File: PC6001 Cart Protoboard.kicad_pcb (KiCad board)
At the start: 2 copper layers, 97.8 x 80.6 mm, 13 parts, among them J1 PC-6001 edge connector, SW1 PicoReset, SW2 EspReset, U2 ESP32-DevKitC, U3 74LS32

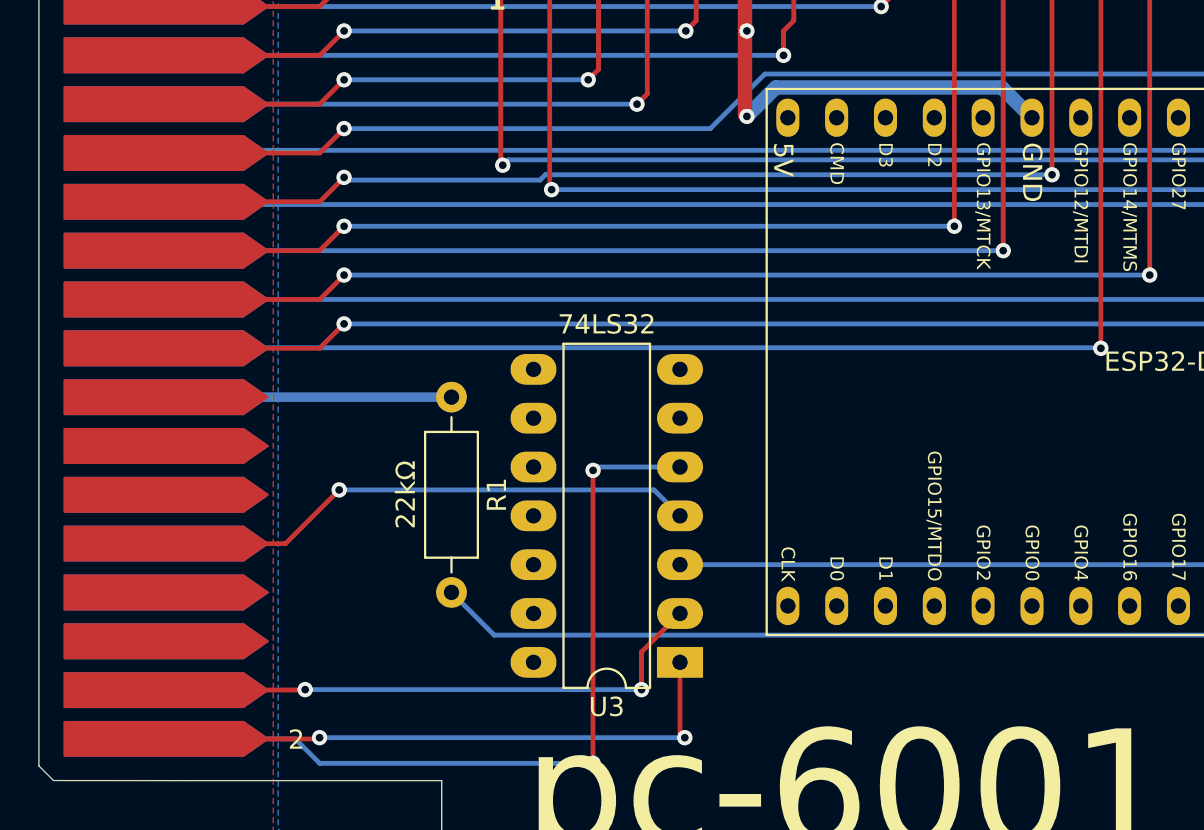
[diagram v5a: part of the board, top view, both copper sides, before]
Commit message: TEMPORARILY putting SRAM in the ESP
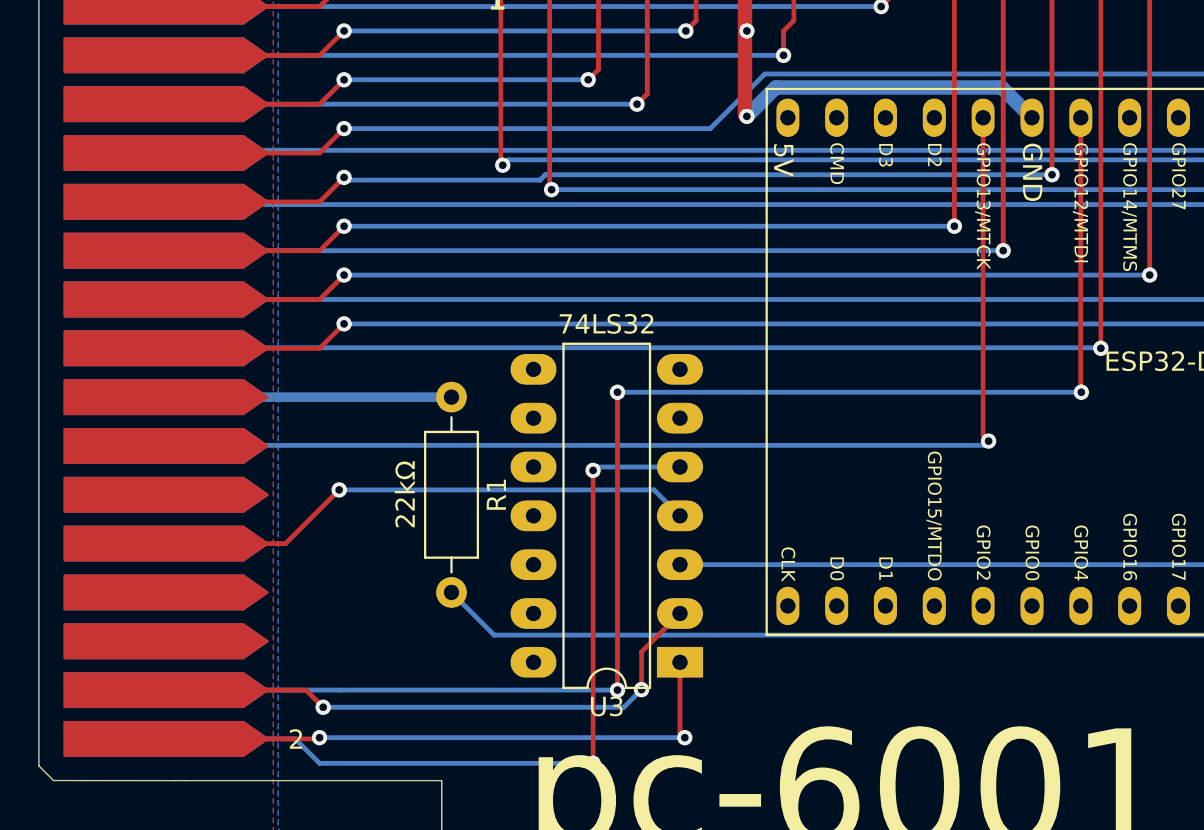
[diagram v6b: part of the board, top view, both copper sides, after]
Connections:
- U2 pad 13: unconnected-(U2-MTDI/GPIO12/ADC2_CH5-Pad13) -> /~{DRD2}
- U2 pad 15: unconnected-(U2-MTCK/GPIO13/ADC2_CH4-Pad15) -> /~{WR}
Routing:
- net /~{DRD2}: track 0.00 -> 80.8 mm, vias 0 -> 3
- net /~{WR}: track 0.00 -> 63.3 mm, vias 0 -> 1
- net /~{CS2}: track 33.0 -> 33.7 mm
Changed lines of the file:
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@@
 	(net 74 "unconnected-(U2-U0RXD{slash}GPIO3-Pad34)")
 	(net 75 "unconnected-(U2-SD_DATA3{slash}GPIO10-Pad17)")
-	(net 76 "unconnected-(U2-MTCK{slash}GPIO13{slash}ADC2_CH4-Pad15)")
-	(net 77 "unconnected-(U2-GPIO18-Pad30)")
-	(net 78 "unconnected-(U2-GPIO19-Pad31)")
-	(net 79 "/WIFI_LED")
-	(net 80 "unconnected-(U2-SD_DATA0{slash}GPIO7-Pad21)")
-	(net 81 "unconnected-(U2-MTMS{slash}GPIO14{slash}ADC2_CH6-Pad12)")
-	(net 82 "/CMD")
-	(net 83 "unconnected-(U2-VDET_2{slash}GPIO35{slash}ADC1_CH7-Pad6)")
-	(net 84 "unconnected-(U2-GPIO0{slash}BOOT{slash}ADC2_CH1-Pad25)")
-	(net 85 "unconnected-(U2-SENSOR_VN{slash}GPIO39{slash}ADC1_CH3-Pad4)")
-	(net 86 "unconnected-(U2-MTDI{slash}GPIO12{slash}ADC2_CH5-Pad13)")
-	(net 87 "unconnected-(U2-SD_DATA2{slash}GPIO9-Pad16)")
-	(net 88 "/ESP_RST")
-	(net 89 "unconnected-(U2-MTDO{slash}GPIO15{slash}ADC2_CH3-Pad23)")
-	(net 90 "+3.3V")
-	(net 91 "Net-(D1-K)")
-	(net 92 "/~{RAMSEL}")
+	(net 76 "unconnected-(U2-GPIO18-Pad30)")
+	(net 77 "unconnected-(U2-GPIO19-Pad31)")
+	(net 78 "/WIFI_LED")
+	(net 79 "unconnected-(U2-SD_DATA0{slash}GPIO7-Pad21)")
+	(net 80 "unconnected-(U2-MTMS{slash}GPIO14{slash}ADC2_CH6-Pad12)")
+	(net 81 "/CMD")
+	(net 82 "unconnected-(U2-VDET_2{slash}GPIO35{slash}ADC1_CH7-Pad6)")
+	(net 83 "unconnected-(U2-GPIO0{slash}BOOT{slash}ADC2_CH1-Pad25)")
+	(net 84 "unconnected-(U2-SENSOR_VN{slash}GPIO39{slash}ADC1_CH3-Pad4)")
+	(net 85 "unconnected-(U2-SD_DATA2{slash}GPIO9-Pad16)")
+	(net 86 "/ESP_RST")
+	(net 87 "unconnected-(U2-MTDO{slash}GPIO15{slash}ADC2_CH3-Pad23)")
+	(net 88 "+3.3V")
+	(net 89 "Net-(D1-K)")
+	(net 90 "/~{RAMSEL}")
 	(footprint "PC6001 Edge Connector:PC6001 Cartridge Connector"
 		(layer "F.Cu")
@@
 		(tags "Diode DO-35_SOD27 series Axial Horizontal pin pitch 7.62mm  length 4mm diameter 2mm")
 		(property "Reference" "D1"
-			(at 3.81 0 360)
+			(at 3.81 0 0)
 			(layer "F.SilkS")
 			(effects
@@
 		)
 		(property "Value" "D"
-			(at 3.81 2.12 360)
+			(at 3.81 2.12 0)
 			(layer "F.Fab")
 			(effects
@@
 		)
 		(fp_text user "${REFERENCE}"
-			(at 4.11 0 360)
+			(at 4.11 0 0)
 			(layer "F.Fab")
 			(effects
@@
 			(layers "*.Cu" "*.Mask")
 			(remove_unused_layers no)
-			(net 91 "Net-(D1-K)")
+			(net 89 "Net-(D1-K)")
 			(pinfunction "K")
 			(pintype "passive")
@@
 			(layers "*.Cu" "*.Mask")
 			(remove_unused_layers no)
-			(net 88 "/ESP_RST")
+			(net 86 "/ESP_RST")
 			(pinfunction "A")
 			(pintype "passive")
@@
 			(layers "*.Cu" "*.Mask")
 			(remove_unused_layers no)
-			(net 91 "Net-(D1-K)")
+			(net 89 "Net-(D1-K)")
 			(pinfunction "2")
 			(pintype "passive")
@@
 			(layers "*.Cu" "*.Mask")
 			(remove_unused_layers no)
-			(net 91 "Net-(D1-K)")
+			(net 89 "Net-(D1-K)")
 			(pinfunction "2")
 			(pintype "passive")
@@
 			(layers "*.Cu" "*.Mask")
 			(remove_unused_layers no)
-			(net 90 "+3.3V")
+			(net 88 "+3.3V")
 			(pinfunction "3V3")
 			(pintype "power_in")
@@
 			(layers "*.Cu" "*.Mask")
 			(remove_unused_layers no)
-			(net 88 "/ESP_RST")
+			(net 86 "/ESP_RST")
 			(pinfunction "CHIP_PU")
 			(pintype "input")
@@
 			(layers "*.Cu" "*.Mask")
 			(remove_unused_layers no)
-			(net 85 "unconnected-(U2-SENSOR_VN{slash}GPIO39{slash}ADC1_CH3-Pad4)")
+			(net 84 "unconnected-(U2-SENSOR_VN{slash}GPIO39{slash}ADC1_CH3-Pad4)")
 			(pinfunction "SENSOR_VN/GPIO39/ADC1_CH3")
 			(pintype "input")
@@
 			(layers "*.Cu" "*.Mask")
 			(remove_unused_layers no)
-			(net 83 "unconnected-(U2-VDET_2{slash}GPIO35{slash}ADC1_CH7-Pad6)")
+			(net 82 "unconnected-(U2-VDET_2{slash}GPIO35{slash}ADC1_CH7-Pad6)")
 			(pinfunction "VDET_2/GPIO35/ADC1_CH7")
 			(pintype "input")
@@
 			(layers "*.Cu" "*.Mask")
 			(remove_unused_layers no)
-			(net 82 "/CMD")
+			(net 81 "/CMD")
 			(pinfunction "DAC_1/ADC2_CH8/GPIO25")
 			(pintype "bidirectional")
@@
 			(layers "*.Cu" "*.Mask")
 			(remove_unused_layers no)
-			(net 81 "unconnected-(U2-MTMS{slash}GPIO14{slash}ADC2_CH6-Pad12)")
+			(net 80 "unconnected-(U2-MTMS{slash}GPIO14{slash}ADC2_CH6-Pad12)")
 			(pinfunction "MTMS/GPIO14/ADC2_CH6")
 			(pintype "bidirectional")
@@
 			(layers "*.Cu" "*.Mask")
 			(remove_unused_layers no)
-			(net 86 "unconnected-(U2-MTDI{slash}GPIO12{slash}ADC2_CH5-Pad13)")
+			(net 4 "/~{DRD2}")
 			(pinfunction "MTDI/GPIO12/ADC2_CH5")
 			(pintype "bidirectional")
@@
 			(layers "*.Cu" "*.Mask")
 			(remove_unused_layers no)
-			(net 76 "unconnected-(U2-MTCK{slash}GPIO13{slash}ADC2_CH4-Pad15)")
+			(net 45 "/~{WR}")
 			(pinfunction "MTCK/GPIO13/ADC2_CH4")
 			(pintype "bidirectional")
@@
 			(layers "*.Cu" "*.Mask")
 			(remove_unused_layers no)
-			(net 87 "unconnected-(U2-SD_DATA2{slash}GPIO9-Pad16)")
+			(net 85 "unconnected-(U2-SD_DATA2{slash}GPIO9-Pad16)")
 			(pinfunction "SD_DATA2/GPIO9")
 			(pintype "bidirectional")
@@
 			(layers "*.Cu" "*.Mask")
 			(remove_unused_layers no)
-			(net 80 "unconnected-(U2-SD_DATA0{slash}GPIO7-Pad21)")
+			(net 79 "unconnected-(U2-SD_DATA0{slash}GPIO7-Pad21)")
 			(pinfunction "SD_DATA0/GPIO7")
 			(pintype "bidirectional")
@@
 			(layers "*.Cu" "*.Mask")
 			(remove_unused_layers no)
-			(net 89 "unconnected-(U2-MTDO{slash}GPIO15{slash}ADC2_CH3-Pad23)")
+			(net 87 "unconnected-(U2-MTDO{slash}GPIO15{slash}ADC2_CH3-Pad23)")
 			(pinfunction "MTDO/GPIO15/ADC2_CH3")
 			(pintype "bidirectional")
@@
 			(layers "*.Cu" "*.Mask")
 			(remove_unused_layers no)
-			(net 79 "/WIFI_LED")
+			(net 78 "/WIFI_LED")
 			(pinfunction "ADC2_CH2/GPIO2")
 			(pintype "bidirectional")
@@
 			(layers "*.Cu" "*.Mask")
 			(remove_unused_layers no)
-			(net 84 "unconnected-(U2-GPIO0{slash}BOOT{slash}ADC2_CH1-Pad25)")
+			(net 83 "unconnected-(U2-GPIO0{slash}BOOT{slash}ADC2_CH1-Pad25)")
 			(pinfunction "GPIO0/BOOT/ADC2_CH1")
 			(pintype "bidirectional")
@@
 			(layers "*.Cu" "*.Mask")
 			(remove_unused_layers no)
-			(net 77 "unconnected-(U2-GPIO18-Pad30)")
+			(net 76 "unconnected-(U2-GPIO18-Pad30)")
 			(pinfunction "GPIO18")
 			(pintype "bidirectional")
@@
 			(layers "*.Cu" "*.Mask")
 			(remove_unused_layers no)
-			(net 78 "unconnected-(U2-GPIO19-Pad31)")
+			(net 77 "unconnected-(U2-GPIO19-Pad31)")
 			(pinfunction "GPIO19")
 			(pintype "bidirectional")
@@
 			(layers "*.Cu" "*.Mask")
 			(remove_unused_layers no)
-			(net 92 "/~{RAMSEL}")
+			(net 90 "/~{RAMSEL}")
 			(pintype "output")
 		)
@@
 			(layers "*.Cu" "*.Mask")
 			(remove_unused_layers no)
-			(net 88 "/ESP_RST")
+			(net 86 "/ESP_RST")
 			(pintype "passive")
 		)
@@
 	)
 	(segment
+		(start 174.85 121.002)
+		(end 174.85 106.75)
+		(width 0.25)
+		(layer "F.Cu")
+		(net 4)
+	)
+	(segment
+		(start 174.879 121.031)
+		(end 174.85 121.002)
+		(width 0.25)
+		(layer "F.Cu")
+		(net 4)
+	)
+	(segment
+		(start 150.749 136.525)
+		(end 150.749 121.031)
+		(width 0.25)
+		(layer "F.Cu")
+		(net 4)
+	)
+	(via
+		(at 150.749 136.525)
+		(size 0.8)
+		(drill 0.4)
+		(layers "F.Cu" "B.Cu")
+		(net 4)
+	)
+	(via
+		(at 174.879 121.031)
+		(size 0.8)
+		(drill 0.4)
+		(layers "F.Cu" "B.Cu")
+		(net 4)
+	)
+	(via
+		(at 150.749 121.031)
+		(size 0.8)
+		(drill 0.4)
+		(layers "F.Cu" "B.Cu")
+		(net 4)
+	)
+	(segment
+		(start 123.825 136.525)
+		(end 136.271 136.525)
+		(width 0.25)
+		(layer "B.Cu")
+		(net 4)
+	)
+	(segment
+		(start 136.271 136.525)
+		(end 150.749 136.525)
+		(width 0.25)
+		(layer "B.Cu")
+		(net 4)
+	)
+	(segment
+		(start 150.749 121.031)
+		(end 174.879 121.031)
+		(width 0.25)
+		(layer "B.Cu")
+		(net 4)
+	)
+	(segment
 		(start 142.113 121.285)
 		(end 123.825 121.285)
@@
 	)
 	(segment
-		(start 134.475 136.525)
-		(end 134.5 136.5)
+		(start 169.77 123.288)
+		(end 169.77 106.75)
 		(width 0.25)
 		(layer "F.Cu")
-		(net 47)
+		(net 45)
+	)
+	(segment
+		(start 170.053 123.571)
+		(end 169.77 123.288)
+		(width 0.25)
+		(layer "F.Cu")
+		(net 45)
+	)
+	(via
+		(at 170.053 123.571)
+		(size 0.8)
+		(drill 0.4)
+		(layers "F.Cu" "B.Cu")
+		(net 45)
+	)
+	(segment
+		(start 123.825 123.825)
+		(end 123.855 123.795)
+		(width 0.25)
+		(layer "B.Cu")
+		(net 45)
+	)
+	(segment
+		(start 123.855 123.795)
+		(end 169.829 123.795)
+		(width 0.25)
+		(layer "B.Cu")
+		(net 45)
+	)
+	(segment
+		(start 169.829 123.795)
+		(end 170.053 123.571)
+		(width 0.25)
+		(layer "B.Cu")
+		(net 45)
 	)
 	(segment
@@
 	(segment
 		(start 123.825 136.525)
-		(end 134.475 136.525)
+		(end 134.543789 136.525)
+		(width 0.25)
+		(layer "F.Cu")
+		(net 47)
+	)
+	(segment
+		(start 134.543789 136.525)
+		(end 135.437901 137.419112)
 		(width 0.25)
 		(layer "F.Cu")
@@
 	)
 	(via
-		(at 134.5 136.5)
+		(at 135.437901 137.419112)
 		(size 0.8)
 		(drill 0.4)
@@
 	)
 	(segment
-		(start 134.5 136.5)
-		(end 152 136.5)
+		(start 152 136.5)
+		(end 151.080888 137.419112)
+		(width 0.25)
+		(layer "B.Cu")
+		(net 47)
+	)
+	(segment
+		(start 151.080888 137.419112)
+		(end 135.437901 137.419112)
 		(width 0.25)
 		(layer "B.Cu")
@@
 		(width 0.25)
 		(layer "F.Cu")
-		(net 88)
+		(net 86)
 	)
 	(segment
@@
 		(width 0.25)
 		(layer "F.Cu")
-		(net 88)
+		(net 86)
 	)
 	(segment
@@
 		(width 0.25)
 		(layer "F.Cu")
-		(net 88)
+		(net 86)
 	)
 	(segment
@@
 		(width 0.25)
 		(layer "F.Cu")
-		(net 88)
+		(net 86)
 	)
 	(via
@@
 		(drill 0.4)
 		(layers "F.Cu" "B.Cu")
-		(net 88)
+		(net 86)
 	)
 	(segment
@@
 		(width 0.25)
 		(layer "B.Cu")
-		(net 88)
+		(net 86)
 	)
 	(segment
@@
 		(width 0.25)
 		(layer "B.Cu")
-		(net 88)
+		(net 86)
 	)
 	(segment
@@
 		(width 0.25)
 		(layer "B.Cu")
-		(net 88)
+		(net 86)
 	)
 	(segment
@@
 		(width 0.25)
 		(layer "F.Cu")
-		(net 91)
+		(net 89)
 	)
 	(segment
@@
 		(width 0.25)
 		(layer "F.Cu")
-		(net 91)
+		(net 89)
 	)
 	(segment
@@
 		(width 0.25)
 		(layer "B.Cu")
-		(net 91)
+		(net 89)
 	)
 	(zone

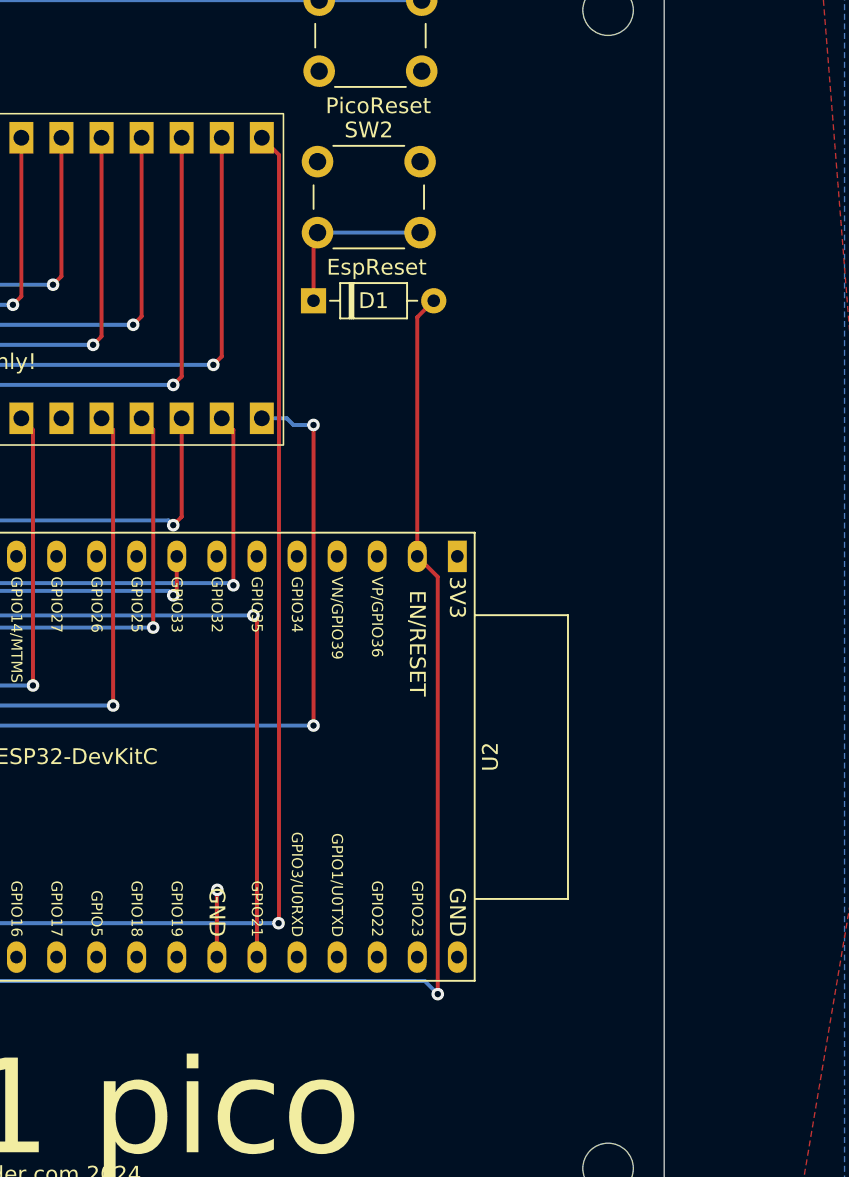
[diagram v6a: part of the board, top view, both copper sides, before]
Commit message: Added an AliExpress microSD card module
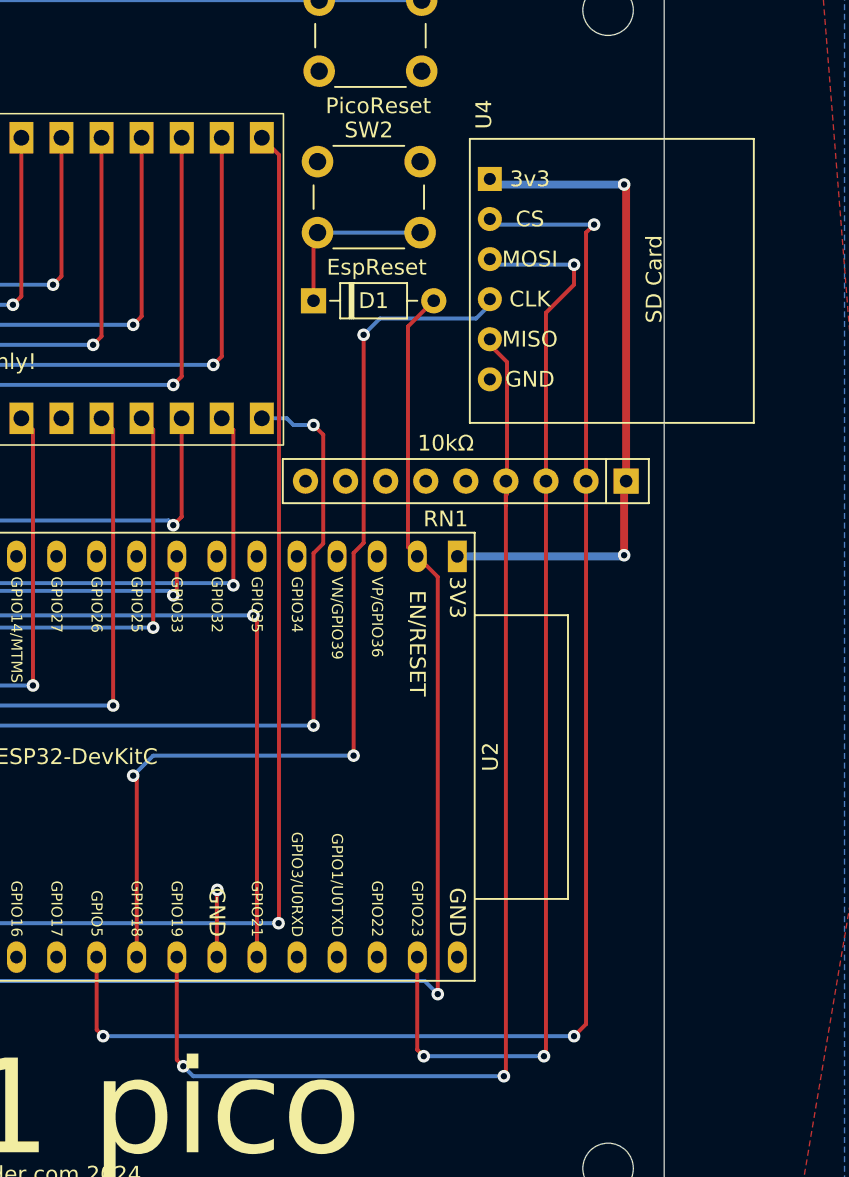
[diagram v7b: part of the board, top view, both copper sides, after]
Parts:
- added RN1: 10kΩ, Resistor_THT:R_Array_SIP9, F.Cu at (216.0, 102.0)
- added U4: microSD-Breakout, microSD_Breakout:microSD_AliExpress, F.Cu at (206.1, 80.3)
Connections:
- U2 pad 29: unconnected-(U2-GPIO5-Pad29) -> /IO5/~{SPI_CS}
- U2 pad 30: unconnected-(U2-GPIO18-Pad30) -> /IO18/SPI_CLK
- U2 pad 31: unconnected-(U2-GPIO19-Pad31) -> /IO19/SPI_MISO
- U2 pad 37: unconnected-(U2-GPIO23-Pad37) -> /IO23/SPI_MOSI
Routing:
- net /IO5/~{SPI_CS}: track 0.00 -> 93.6 mm, vias 0 -> 3
- net /IO19/SPI_MISO: track 0.00 -> 76.1 mm, vias 0 -> 2
- net /IO23/SPI_MOSI: track 0.00 -> 70.4 mm, vias 0 -> 3
- net /IO18/SPI_CLK: track 0.00 -> 61.8 mm, vias 0 -> 3
- net +3.3V: track 0.00 -> 42.7 mm, vias 0 -> 2
- net /a15: track 95.4 -> 95.9 mm

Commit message: Button A
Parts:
- added D2: Wifi, LED_THT:LED_D3.0mm, F.Cu at (214.6, 130.8)
- added D3: Bus, LED_THT:LED_D3.0mm, F.Cu at (214.6, 138.4)
- added R2: 560Ω, Resistor_THT:R_Axial_DIN0207_L6.3mm_D2.5mm_P10.16mm_Horizontal, F.Cu at (198.8, 140.3)
- added R3: 560Ω, Resistor_THT:R_Axial_DIN0207_L6.3mm_D2.5mm_P10.16mm_Horizontal, F.Cu at (198.8, 143.5)
- added SW3: Button A, Button_Switch_THT:SW_PUSH_6mm, F.Cu at (151.1, 70.8)
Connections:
- RN1 pad 5: unconnected-(RN1-R4-Pad5) -> /IO0/BUTTON_A
- U2 pad 12: unconnected-(U2-MTMS/GPIO14/ADC2_CH6-Pad12) -> /~{RAMSEL}
- U2 pad 25: unconnected-(U2-GPIO0/BOOT/ADC2_CH1-Pad25) -> /IO0/BUTTON_A
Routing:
- net /IO0/BUTTON_A: track 0.00 -> 169.1 mm, vias 0 -> 5
- net /BUS_LED: track 0.00 -> 54.9 mm, vias 0 -> 4
- net /WIFI_LED: track 0.00 -> 50.8 mm, vias 0 -> 1
- net GND: track 54.0 -> 94.7 mm, vias 3 -> 5
- net /~{RAMSEL}: track 0.00 -> 38.6 mm, vias 0 -> 1
- net Net-(D2-K): track 0.00 -> 17.0 mm, vias 0 -> 1
- net Net-(D3-K): track 0.00 -> 10.4 mm, vias 0 -> 1
- net /IO19/SPI_MISO: track 76.1 -> 77.8 mm
